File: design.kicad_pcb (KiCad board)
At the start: 2 copper layers, 0 parts

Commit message: Update design.kicad_pcb
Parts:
- added C1: C_Small, Capacitor_SMD:C_0805_2012Metric, F.Cu at (141.0, 81.0)
- added C2: C_Small, Capacitor_SMD:C_0805_2012Metric, F.Cu at (120.2, 102.5)
- added C3: C_Small, Capacitor_SMD:C_0805_2012Metric, F.Cu at (128.3, 92.7)
- added C4: 1uF, Capacitor_SMD:C_0805_2012Metric, F.Cu at (134.2, 88.0)
- added C5: 10uF, Capacitor_SMD:C_0805_2012Metric, F.Cu at (128.3, 95.7)
- added C6: 0.1uF, Capacitor_SMD:C_0805_2012Metric, F.Cu at (111.3, 102.5)
- added C7: 100nF, Capacitor_SMD:C_0805_2012Metric, F.Cu at (115.7, 102.5)
- added C8: 0-50pF, Capacitor_SMD:C_0805_2012Metric, F.Cu at (106.8, 102.5)
- added JP1: TOG, Jumper:SolderJumper-2_P1.3mm_Open_RoundedPad1.0x1.5mm, F.Cu at (128.2, 99.0)
- added JP2: AHLB, Jumper:SolderJumper-2_P1.3mm_Bridged_RoundedPad1.0x1.5mm, F.Cu at (145.4, 81.3)
- added L1: L_Small, Inductor_SMD:L_TracoPower_TCK-047_5.2x5.8mm, F.Cu at (129.8, 83.0)
- added R1: R_Small, Resistor_SMD:R_0805_2012Metric, F.Cu at (141.0, 84.0)
- added R2: R_Small, Resistor_SMD:R_0805_2012Metric, F.Cu at (132.7, 92.7)
- added R3: 10K, Resistor_SMD:R_0805_2012Metric, F.Cu at (138.6, 86.9)
- added U2: AP3015, Package_TO_SOT_SMD:SOT-23-5, F.Cu at (136.2, 81.7)
- added U3: ESP32-C3-WROOM-02-N4, MCU_Espressif_custom:MODULE_ESP32-C3-WROOM-02-H4, F.Cu at (115.8, 90.3)
- added U4: TTP223, Package_TO_SOT_SMD:SOT-23-6_Handsoldering, F.Cu at (129.0, 88.9)

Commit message: Update design.kicad_pcb
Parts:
- added U1: TCK127BG, Package_BGA_custom:Toshiba_WCSP4G, F.Cu at (136.0, 98.0)

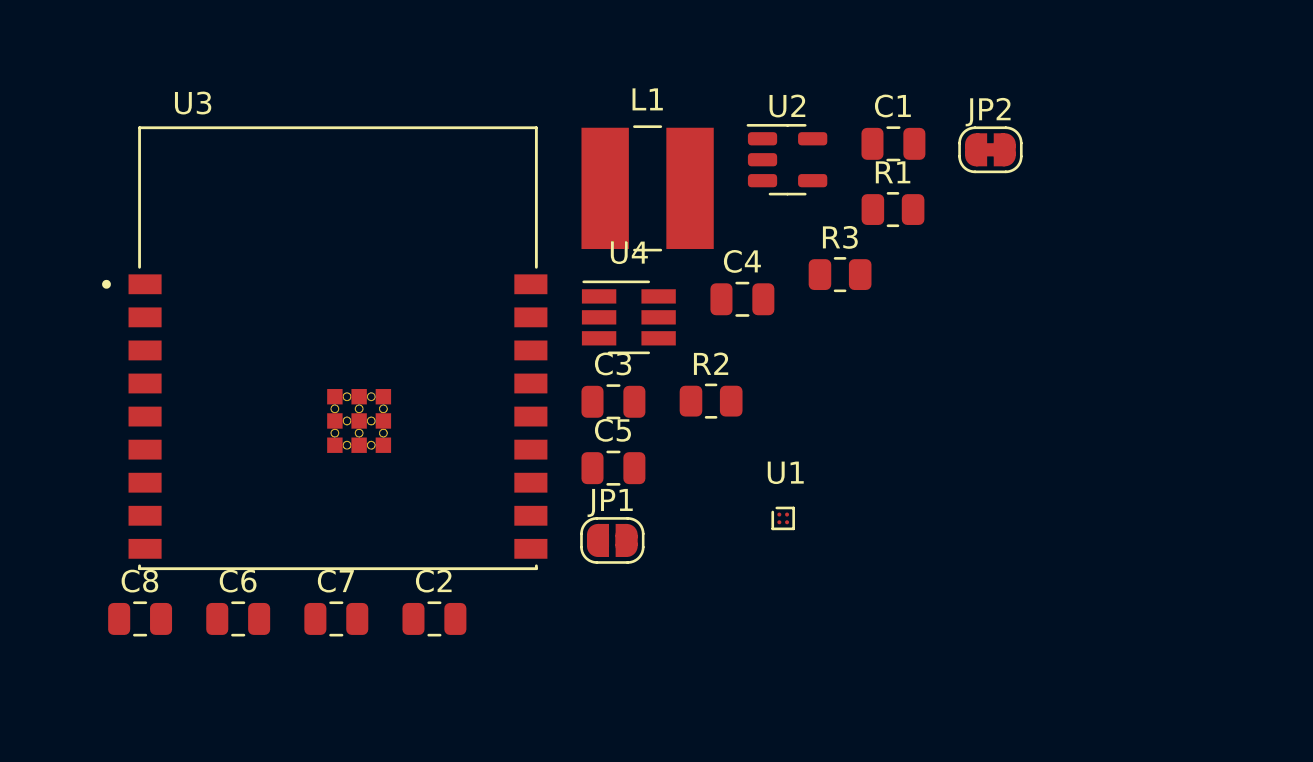
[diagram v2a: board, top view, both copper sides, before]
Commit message: PCB outline
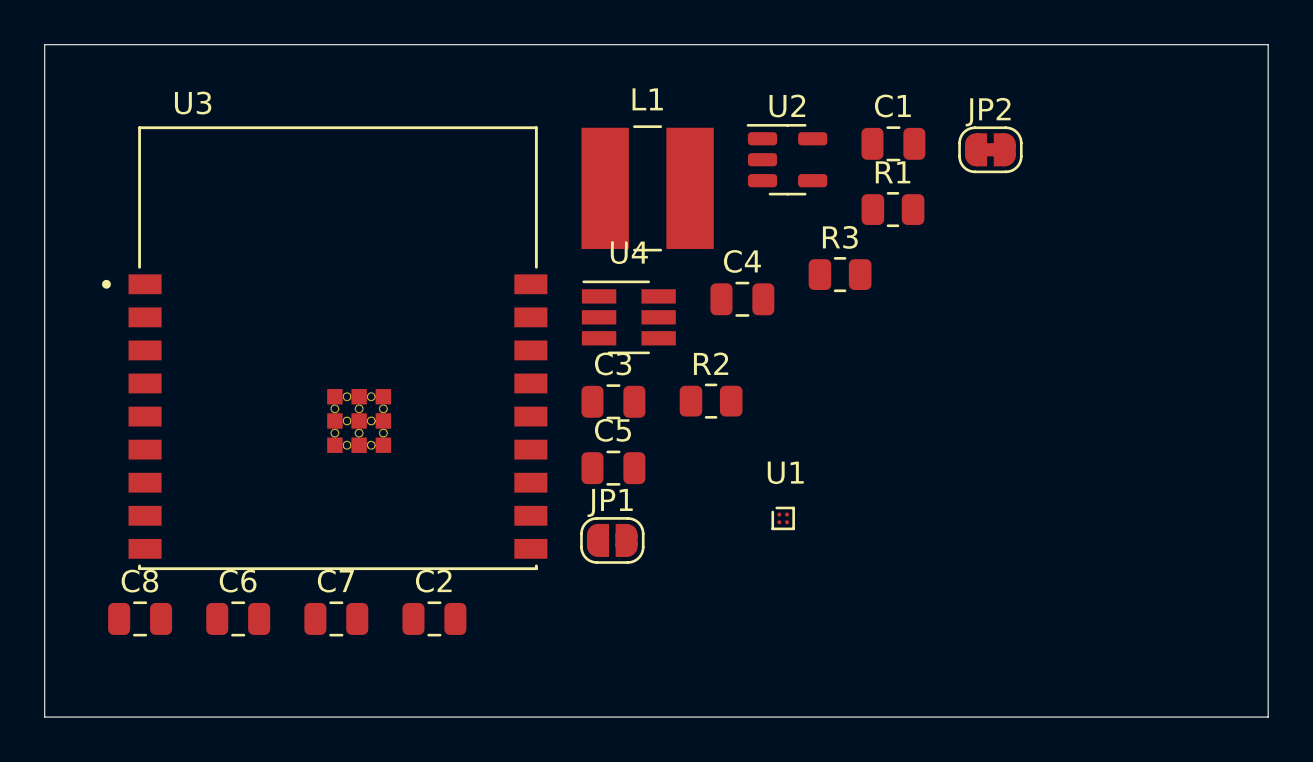
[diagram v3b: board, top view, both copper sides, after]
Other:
- board outline added: 55.5 x 30.5 mm
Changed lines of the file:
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@@
     )
   )
+  (gr_rect (start 158 107) (end 102.5 76.5) (layer "Edge.Cuts") (width 0.05) (fill none))
   (gr_text "<<project_name>>\n<<ID>>\n<<version>>\n<<date>>\n<<hash>>\n<<website_link>>" (at 146.5 95.504) (layer "B.SilkS")
     (effects (font (size 1 1) (thickness 0.15)) (justify mirror))
